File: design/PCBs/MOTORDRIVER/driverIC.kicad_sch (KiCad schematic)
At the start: 19 parts, among them U1 TMC4671-LA

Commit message: Removed unneccessary TMC4761 pins
Finally went through every pin on the TMC and tried to eliminate
unneeded pins. Reduced sheet complexity quite nicely. Pretty much
all rationales for removing pins were added to the design document,
although not formatted that nicely yet.
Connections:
- net BRAKE: no longer names the net of U1.31 (BRAKE)
- net DIR: no longer names the net of U1.56 (DIR)
- net ENO: no longer names the net of U1.32 (ENO)
- net GPIO_0: no longer names the net of U1.70 (GPIO0/ADC_I0_MCD)
- net GPIO_1: no longer names the net of U1.71 (GPIO1/ADC_I1_MCD)
- net GPIO_2: no longer names the net of U1.74 (GPIO2/ADC_VM_MCD)
- net GPIO_3 renamed GPIO3
- net GPIO_4 renamed GPIO4
- net PWM_I: no longer names the net of U1.58 (PWM_I)
- net PWM_IDLE_H: no longer names the net of U1.59 (PWM_IDLE_H)
- net PWM_IDLE_L: no longer names the net of U1.60 (PWM_IDLE_L)
- net REF_H: no longer names the net of U1.68 (REF_H)
- net REF_L: no longer names the net of U1.67 (REF_L)
- net REF_R: no longer names the net of U1.69 (REF_R)
- net STP: no longer names the net of U1.57 (STP)
- net TMC_UART_RX: no longer names the net of U1.10 (UART_RXD)
- net TMC_UART_TX: no longer names the net of U1.11 (UART_TXD)
- no-connect marks 12 -> 25
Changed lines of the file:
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@@
+	)
+	(no_connect
+		(at 227.33 54.61)
 	)
 	(no_connect
@@
 	)
 	(no_connect
+		(at 227.33 90.17)
+	)
+	(no_connect
+		(at 227.33 92.71)
+	)
+	(no_connect
 		(at 80.01 90.17)
 	)
 	(no_connect
+		(at 80.01 118.11)
+	)
+	(no_connect
+		(at 227.33 64.77)
+	)
+	(no_connect
 		(at 80.01 92.71)
 	)
 	(no_connect
+		(at 80.01 64.77)
+	)
+	(no_connect
+		(at 80.01 115.57)
+	)
+	(no_connect
 		(at 227.33 39.37)
 	)
 	(no_connect
+		(at 227.33 59.69)
+	)
+	(no_connect
+		(at 80.01 62.23)
+	)
+	(no_connect
+		(at 227.33 87.63)
+	)
+	(no_connect
 		(at 80.01 123.19)
 	)
@@
 	)
 	(no_connect
+		(at 227.33 46.99)
+	)
+	(no_connect
+		(at 227.33 62.23)
+	)
+	(no_connect
 		(at 227.33 72.39)
+	)
+	(no_connect
+		(at 227.33 57.15)
 	)
 	(wire
@@
 		)
 	)
-	(hierarchical_label "BRAKE"
-		(shape input)
-		(at 80.01 115.57 180)
-		(fields_autoplaced yes)
-		(effects
-			(font
-				(size 1.27 1.27)
-			)
-			(justify right)
-		)
-	)
 	(hierarchical_label "ADC_I1_NEG"
 		(shape input)
@@
 		)
 	)
-	(hierarchical_label "PWM_I"
-		(shape input)
-		(at 227.33 87.63 0)
-		(fields_autoplaced yes)
-		(effects
-			(font
-				(size 1.27 1.27)
-			)
-			(justify left)
-		)
-	)
-	(hierarchical_label "STP"
-		(shape input)
-		(at 227.33 90.17 0)
-		(fields_autoplaced yes)
-		(effects
-			(font
-				(size 1.27 1.27)
-			)
-			(justify left)
-		)
-	)
 	(hierarchical_label "AENC_WY_POS"
 		(shape input)
@@
 		)
 	)
-	(hierarchical_label "PWM_IDLE_H"
-		(shape input)
-		(at 227.33 85.09 0)
-		(fields_autoplaced yes)
-		(effects
-			(font
-				(size 1.27 1.27)
-			)
-			(justify left)
-		)
-	)
-	(hierarchical_label "REF_L"
-		(shape input)
-		(at 227.33 64.77 0)
-		(fields_autoplaced yes)
-		(effects
-			(font
-				(size 1.27 1.27)
-			)
-			(justify left)
-		)
-	)
 	(hierarchical_label "GPIO7"
 		(shape input)
@@
 		)
 	)
-	(hierarchical_label "GPIO_4"
+	(hierarchical_label "GPIO4"
 		(shape input)
 		(at 227.33 41.91 0)
@@
 		)
 	)
-	(hierarchical_label "REF_R"
-		(shape input)
-		(at 227.33 59.69 0)
-		(fields_autoplaced yes)
-		(effects
-			(font
-				(size 1.27 1.27)
-			)
-			(justify left)
-		)
-	)
 	(hierarchical_label "AENC_UX_POS"
 		(shape input)
@@
 		)
 	)
-	(hierarchical_label "GPIO_3"
+	(hierarchical_label "GPIO3"
 		(shape input)
 		(at 227.33 44.45 0)
@@
 		)
 	)
-	(hierarchical_label "DIR"
-		(shape input)
-		(at 227.33 92.71 0)
-		(fields_autoplaced yes)
-		(effects
-			(font
-				(size 1.27 1.27)
-			)
-			(justify left)
-		)
-	)
 	(hierarchical_label "PWM_W1_H"
 		(shape input)
@@
 		)
 	)
-	(hierarchical_label "GPIO_2"
-		(shape input)
-		(at 227.33 46.99 0)
-		(fields_autoplaced yes)
-		(effects
-			(font
-				(size 1.27 1.27)
-			)
-			(justify left)
-		)
-	)
-	(hierarchical_label "GPIO_0"
-		(shape input)
-		(at 227.33 57.15 0)
-		(fields_autoplaced yes)
-		(effects
-			(font
-				(size 1.27 1.27)
-			)
-			(justify left)
-		)
-	)
 	(hierarchical_label "ADC_I0_NEG"
 		(shape input)
@@
 		)
 	)
-	(hierarchical_label "ENO"
-		(shape input)
-		(at 80.01 118.11 180)
-		(fields_autoplaced yes)
-		(effects
-			(font
-				(size 1.27 1.27)
-			)
-			(justify right)
-		)
-	)
 	(hierarchical_label "AENC_VN_POS"
 		(shape input)
@@
 		)
 	)
-	(hierarchical_label "REF_H"
-		(shape input)
-		(at 227.33 62.23 0)
-		(fields_autoplaced yes)
-		(effects
-			(font
-				(size 1.27 1.27)
-			)
-			(justify left)
-		)
-	)
-	(hierarchical_label "TMC_UART_RX"
-		(shape input)
-		(at 80.01 62.23 180)
-		(fields_autoplaced yes)
-		(effects
-			(font
-				(size 1.27 1.27)
-			)
-			(justify right)
-		)
-	)
 	(hierarchical_label "GPIO5"
 		(shape input)
@@
 		)
 	)
-	(hierarchical_label "PWM_IDLE_L"
-		(shape input)
-		(at 227.33 82.55 0)
-		(fields_autoplaced yes)
-		(effects
-			(font
-				(size 1.27 1.27)
-			)
-			(justify left)
-		)
-	)
-	(hierarchical_label "TMC_UART_TX"
-		(shape input)
-		(at 80.01 64.77 180)
-		(fields_autoplaced yes)
-		(effects
-			(font
-				(size 1.27 1.27)
-			)
-			(justify right)
-		)
-	)
 	(hierarchical_label "STATUS"
 		(shape input)
@@
 		)
 	)
-	(hierarchical_label "GPIO_1"
-		(shape input)
-		(at 227.33 54.61 0)
-		(fields_autoplaced yes)
-		(effects
-			(font
-				(size 1.27 1.27)
-			)
-			(justify left)
-		)
-	)

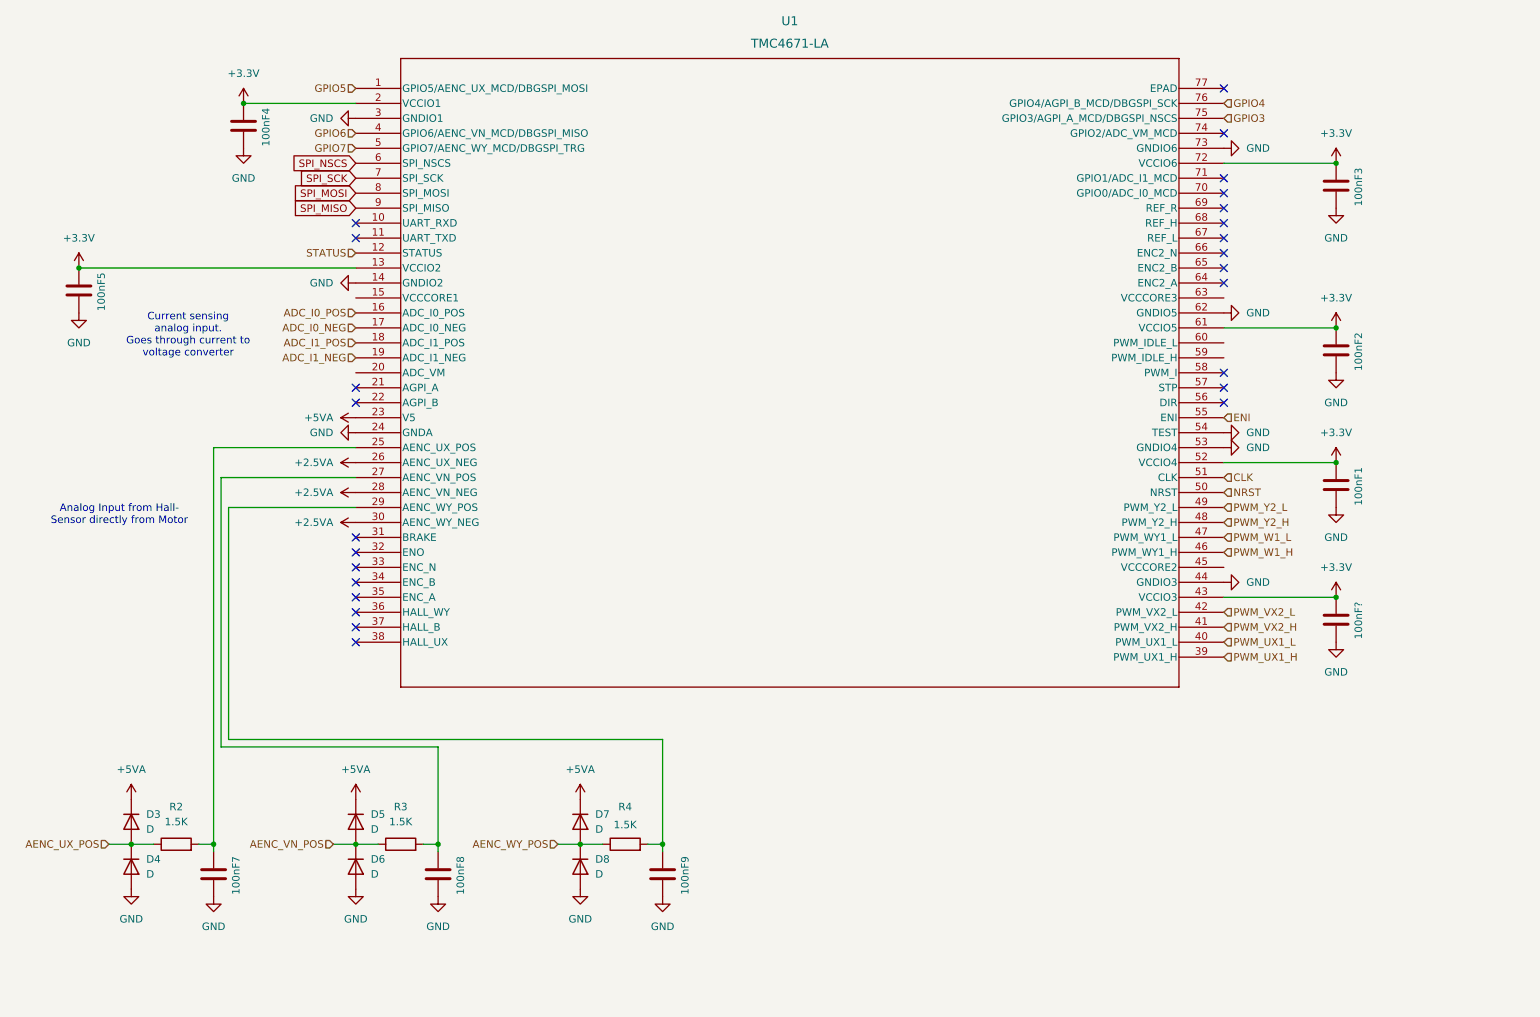
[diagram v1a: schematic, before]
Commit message: Switched TMC hall sensor input to digital from motors
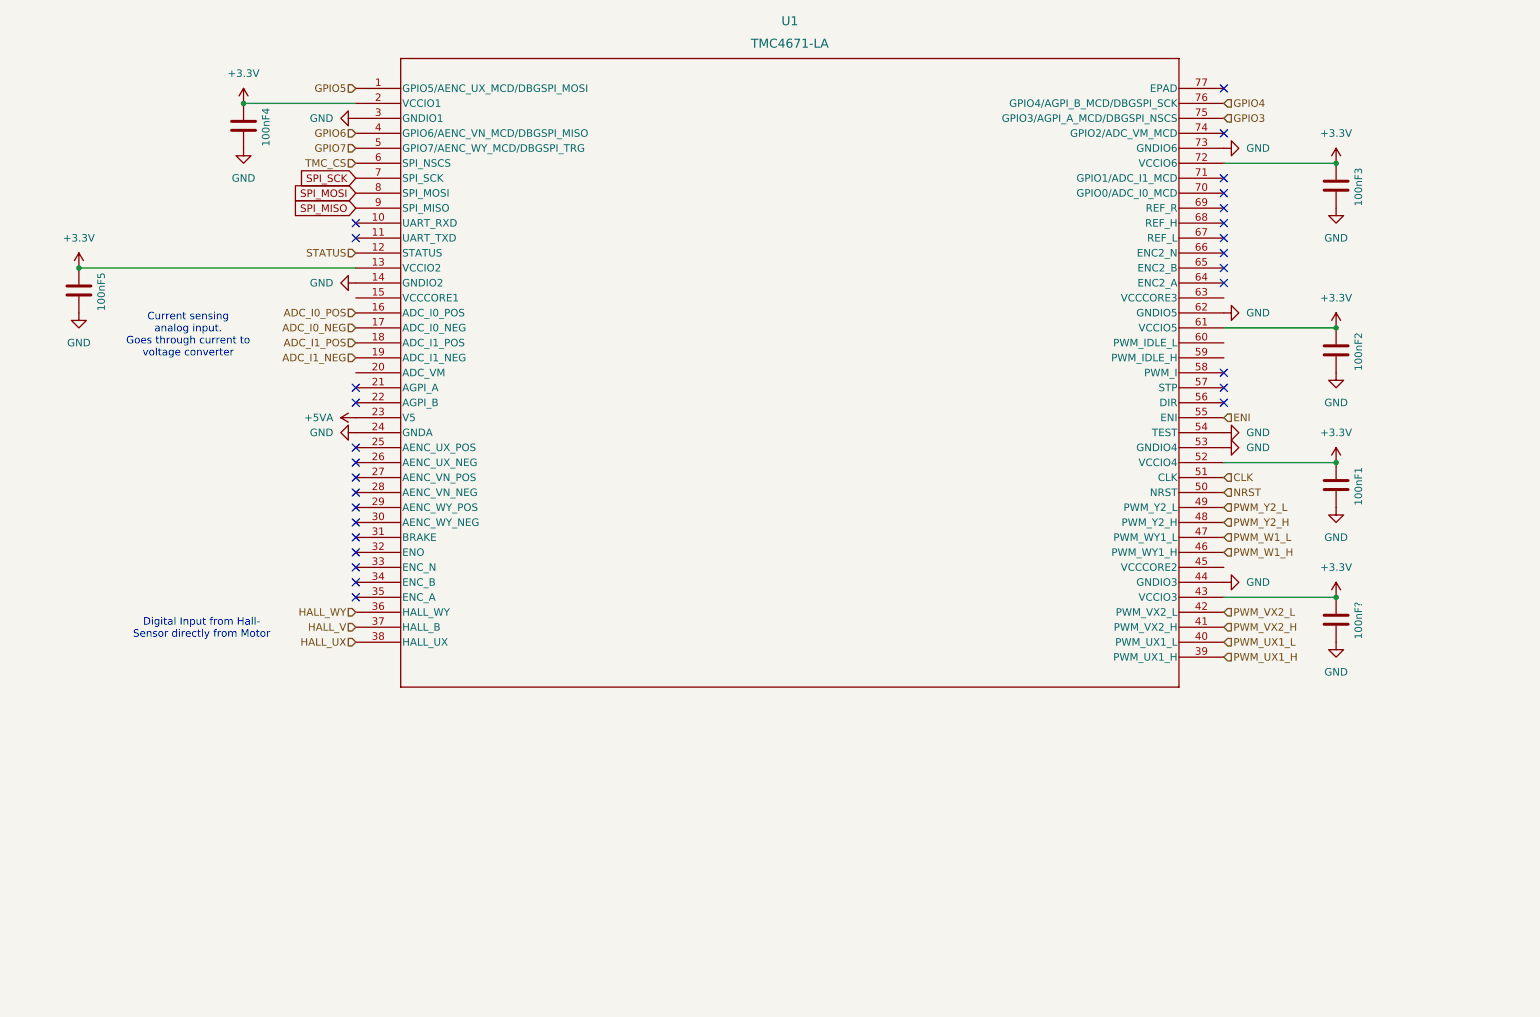
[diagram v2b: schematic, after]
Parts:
- removed 100nF7, 100nF8, 100nF9: C, symbol Device:C
- removed D3, D4, D5, D6, D7, D8: D, symbol Device:D
- removed R2, R3, R4: 1.5K, symbol Device:R
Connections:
- net HALL_WY: now reaches U1.36 (HALL_WY)
- net HALL_V: now reaches U1.37 (HALL_B)
- net HALL_UX: now reaches U1.38 (HALL_UX)
- removed net +2.5VA: U1.26 (AENC_UX_NEG), U1.28 (AENC_VN_NEG), U1.30 (AENC_WY_NEG)
- net SPI_NSCS renamed TMC_CS
- no-connect marks 25 -> 28
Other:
- note added: "Digital Input from Hall- Sensor directly from Motor"
- note removed: "Analog Input from Hall- Sensor directly from Motor"

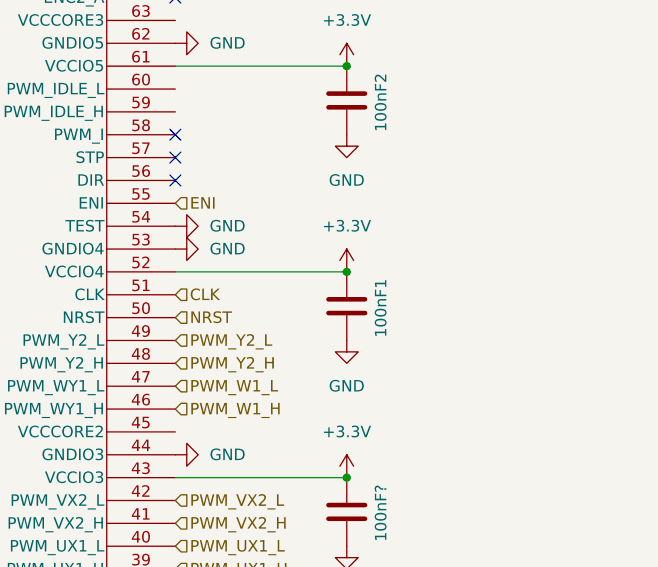
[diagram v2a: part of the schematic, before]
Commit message: TMC and MCU connections
Further progress on PCB. Main remainders are:

Voltage regulator page  (couple todos)
Fix sheet duplication for output sheets
Decide on UART or SPI debug for TMC
Formalize stuff, fill out bottom right on sheets
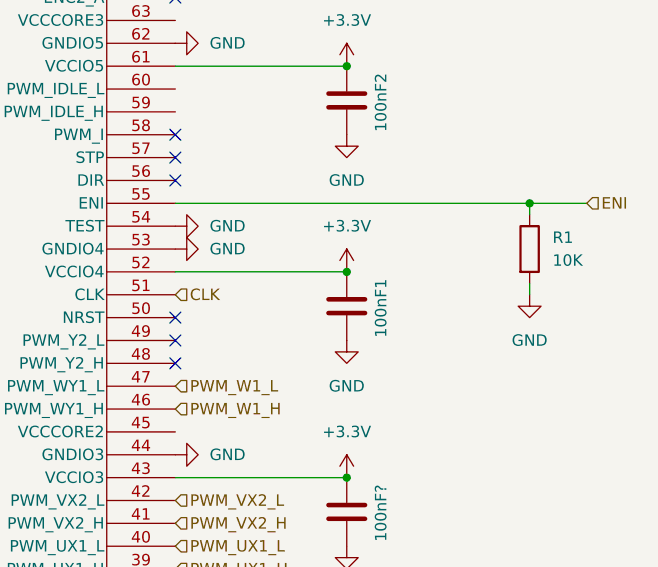
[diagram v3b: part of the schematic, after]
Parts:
- added R1: 10K, symbol Device:R
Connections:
- net ENI: now also R1.1
- net GND: now also R1.2
- net NRST: no longer names the net of U1.50 (NRST)
- net PWM_Y2_H: no longer names the net of U1.48 (PWM_Y2_H)
- net PWM_Y2_L: no longer names the net of U1.49 (PWM_Y2_L)
- no-connect marks 28 -> 31
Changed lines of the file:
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@@
+	)
+	(junction
+		(at 266.7 95.25)
+		(diameter 0)
+		(color 0 0 0 0)
 	)
 	(junction
@@
 	)
 	(no_connect
+		(at 227.33 107.95)
+	)
+	(no_connect
 		(at 80.01 125.73)
 	)
@@
 	)
 	(no_connect
+		(at 227.33 110.49)
+	)
+	(no_connect
 		(at 227.33 39.37)
 	)
@@
 	)
 	(no_connect
+		(at 227.33 113.03)
+	)
+	(no_connect
 		(at 227.33 62.23)
 	)
@@
 	(no_connect
 		(at 80.01 107.95)
+	)
+	(wire
+		(pts
+			(xy 227.33 95.25) (xy 266.7 95.25)
+		)
+		(stroke
+			(width 0)
+			(type default)
+		)
+	)
+	(wire
+		(pts
+			(xy 266.7 95.25) (xy 266.7 96.52)
+		)
+		(stroke
+			(width 0)
+			(type default)
+		)
 	)
 	(wire
@@
 	(wire
 		(pts
-			(xy 227.33 102.87) (xy 246.38 102.87)
+			(xy 266.7 104.14) (xy 266.7 105.41)
 		)
 		(stroke
@@
 	(wire
 		(pts
-			(xy 227.33 125.73) (xy 246.38 125.73)
+			(xy 227.33 102.87) (xy 246.38 102.87)
 		)
 		(stroke
@@
 	(wire
 		(pts
-			(xy 227.33 52.07) (xy 246.38 52.07)
+			(xy 266.7 95.25) (xy 273.05 95.25)
 		)
 		(stroke
@@
 		)
 	)
+	(wire
+		(pts
+			(xy 227.33 125.73) (xy 246.38 125.73)
+		)
+		(stroke
+			(width 0)
+			(type default)
+		)
+	)
+	(wire
+		(pts
+			(xy 227.33 52.07) (xy 246.38 52.07)
+		)
+		(stroke
+			(width 0)
+			(type default)
+		)
+	)
 	(text "Current sensing\nanalog input. \nGoes through current to\nvoltage converter\n"
 		(exclude_from_sim no)
@@
 	(hierarchical_label "ENI"
 		(shape input)
-		(at 227.33 95.25 0)
+		(at 273.05 95.25 0)
 		(fields_autoplaced yes)
 		(effects
@@
 		)
 	)
-	(hierarchical_label "NRST"
-		(shape input)
-		(at 227.33 107.95 0)
+	(hierarchical_label "ADC_I0_NEG"
+		(shape input)
+		(at 80.01 80.01 180)
+		(fields_autoplaced yes)
+		(effects
+			(font
+				(size 1.27 1.27)
+			)
+			(justify right)
+		)
+	)
+	(hierarchical_label "GPIO5"
+		(shape input)
+		(at 80.01 39.37 180)
+		(fields_autoplaced yes)
+		(effects
+			(font
+				(size 1.27 1.27)
+			)
+			(justify right)
+		)
+	)
+	(hierarchical_label "CLK"
+		(shape input)
+		(at 227.33 105.41 0)
 		(fields_autoplaced yes)
 		(effects
@@
 		)
 	)
-	(hierarchical_label "PWM_Y2_H"
-		(shape input)
-		(at 227.33 113.03 0)
+	(hierarchical_label "GPIO6"
+		(shape input)
+		(at 80.01 46.99 180)
+		(fields_autoplaced yes)
+		(effects
+			(font
+				(size 1.27 1.27)
+			)
+			(justify right)
+		)
+	)
+	(hierarchical_label "PWM_UX1_H"
+		(shape input)
+		(at 227.33 135.89 0)
 		(fields_autoplaced yes)
 		(effects
@@
 		)
 	)
-	(hierarchical_label "ADC_I0_NEG"
-		(shape input)
-		(at 80.01 80.01 180)
+	(hierarchical_label "HALL_WY"
+		(shape input)
+		(at 80.01 128.27 180)
 		(fields_autoplaced yes)
 		(effects
@@
 		)
 	)
-	(hierarchical_label "PWM_Y2_L"
-		(shape input)
-		(at 227.33 110.49 0)
-		(fields_autoplaced yes)
-		(effects
-			(font
-				(size 1.27 1.27)
-			)
-			(justify left)
-		)
-	)
-	(hierarchical_label "GPIO5"
-		(shape input)
-		(at 80.01 39.37 180)
+	(hierarchical_label "HALL_V"
+		(shape input)
+		(at 80.01 130.81 180)
 		(fields_autoplaced yes)
 		(effects
@@
 		)
 	)
-	(hierarchical_label "CLK"
-		(shape input)
-		(at 227.33 105.41 0)
-		(fields_autoplaced yes)
-		(effects
-			(font
-				(size 1.27 1.27)
-			)
-			(justify left)
-		)
-	)
-	(hierarchical_label "GPIO6"
-		(shape input)
-		(at 80.01 46.99 180)
+	(hierarchical_label "STATUS"
+		(shape input)
+		(at 80.01 67.31 180)
 		(fields_autoplaced yes)
 		(effects
@@
 		)
 	)
-	(hierarchical_label "PWM_UX1_H"
-		(shape input)
-		(at 227.33 135.89 0)
-		(fields_autoplaced yes)
-		(effects
-			(font
-				(size 1.27 1.27)
-			)
-			(justify left)
-		)
-	)
-	(hierarchical_label "HALL_WY"
-		(shape input)
-		(at 80.01 128.27 180)
-		(fields_autoplaced yes)
-		(effects
-			(font
-				(size 1.27 1.27)
-			)
-			(justify right)
-		)
-	)
-	(hierarchical_label "HALL_V"
-		(shape input)
-		(at 80.01 130.81 180)
-		(fields_autoplaced yes)
-		(effects
-			(font
-				(size 1.27 1.27)
-			)
-			(justify right)
-		)
-	)
-	(hierarchical_label "STATUS"
-		(shape input)
-		(at 80.01 67.31 180)
-		(fields_autoplaced yes)
-		(effects
-			(font
-				(size 1.27 1.27)
-			)
-			(justify right)
+	(symbol
+		(lib_id "power:GND")
+		(at 266.7 105.41 0)
+		(unit 1)
+		(exclude_from_sim no)
+		(in_bom yes)
+		(on_board yes)
+		(dnp no)
+		(fields_autoplaced yes)
+		(property "Reference" "#PWR06"
+			(at 266.7 111.76 0)
+			(effects
+				(font
+					(size 1.27 1.27)
+				)
+				(hide yes)
+			)
+		)
+		(property "Value" "GND"
+			(at 266.7 110.49 0)
+			(effects
+				(font
+					(size 1.27 1.27)
+				)
+			)
+		)
+		(property "Footprint" ""
+			(at 266.7 105.41 0)
+			(effects
+				(font
+					(size 1.27 1.27)
+				)
+				(hide yes)
+			)
+		)
+		(property "Datasheet" ""
+			(at 266.7 105.41 0)
+			(effects
+				(font
+					(size 1.27 1.27)
+				)
+				(hide yes)
+			)
+		)
+		(property "Description" "Power symbol creates a global label with name \"GND\" , ground"
+			(at 266.7 105.41 0)
+			(effects
+				(font
+					(size 1.27 1.27)
+				)
+				(hide yes)
+			)
+		)
+		(pin "1"
+		)
+		(instances
+			(project ""
+				(path "/c7634e88-16d1-45ec-9aac-9c841e03cf6d/095cf403-627e-473d-974a-cb1fe8ca8b1f"
+					(reference "#PWR06")
+					(unit 1)
+				)
+				(path "/c7634e88-16d1-45ec-9aac-9c841e03cf6d/3a57148f-9ebd-4906-ad6b-7dbf7876a4a8"
+					(reference "#PWR08")
+					(unit 1)
+				)
+				(path "/c7634e88-16d1-45ec-9aac-9c841e03cf6d/acd3f6cb-f2e2-4fe4-b3cb-86a86a6f231d"
+					(reference "#PWR07")
+					(unit 1)
+				)
+			)
 		)
 	)
@@
 					(unit 1)
 				)
+			)
+		)
+	)
+	(symbol
+		(lib_id "Device:R")
+		(at 266.7 100.33 0)
+		(unit 1)
+		(exclude_from_sim no)
+		(in_bom yes)
+		(on_board yes)
+		(dnp no)
+		(fields_autoplaced yes)
+		(property "Reference" "R1"
+			(at 269.24 99.0599 0)
+			(effects
+				(font
+					(size 1.27 1.27)
+				)
+				(justify left)
+			)
+		)
+		(property "Value" "10K"
+			(at 269.24 101.5999 0)
+			(effects
+				(font
+					(size 1.27 1.27)
+				)
+				(justify left)
+			)
+		)
+		(property "Footprint" ""
+			(at 264.922 100.33 90)
+			(effects
+				(font
+					(size 1.27 1.27)
+				)
+				(hide yes)
+			)
+		)
+		(property "Datasheet" "~"
+			(at 266.7 100.33 0)
+			(effects
+				(font
+					(size 1.27 1.27)
+				)
+				(hide yes)
+			)
+		)
+		(property "Description" "Resistor"
+			(at 266.7 100.33 0)
+			(effects
+				(font
+					(size 1.27 1.27)
+				)
+				(hide yes)
+			)
+		)
+		(pin "1"
+		)
+		(pin "2"
+		)
+		(instances
+			(project ""
+				(path "/c7634e88-16d1-45ec-9aac-9c841e03cf6d/095cf403-627e-473d-974a-cb1fe8ca8b1f"
+					(reference "R1")
+					(unit 1)
+				)
+				(path "/c7634e88-16d1-45ec-9aac-9c841e03cf6d/3a57148f-9ebd-4906-ad6b-7dbf7876a4a8"
+					(reference "R3")
+					(unit 1)
+				)
+				(path "/c7634e88-16d1-45ec-9aac-9c841e03cf6d/acd3f6cb-f2e2-4fe4-b3cb-86a86a6f231d"
+					(reference "R2")
+					(unit 1)
+				)

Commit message: documentation, values, double-checking stuff
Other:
- note added: "1.0"
- note added: "2024-12-14"
- note added: "driver IC"
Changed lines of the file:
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@@
+		)
+	)
+	(text "driver IC"
+		(exclude_from_sim no)
+		(at 194.818 190.246 0)
+		(effects
+			(font
+				(size 1.27 1.27)
+			)
 		)
 	)
@@
 		(effects
 			(font
+				(size 1.27 1.27)
+			)
+		)
+	)
+	(text "2024-12-14"
+		(exclude_from_sim no)
+		(at 212.852 193.802 0)
+		(effects
+			(font
+				(size 1.27 1.27)
+			)
+		)
+	)
+	(text "1.0"
+		(exclude_from_sim no)
+		(at 270.764 193.802 0)
+		(effects
+			(font
